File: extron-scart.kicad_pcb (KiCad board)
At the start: 2 copper layers, 17 x 61 mm, 6 parts, among them J1 SCART-F, J2 Conn_Coaxial, J3 Conn_Coaxial, J4 Conn_Coaxial, J5 Conn_Coaxial, J6 Conn_01x03_Male

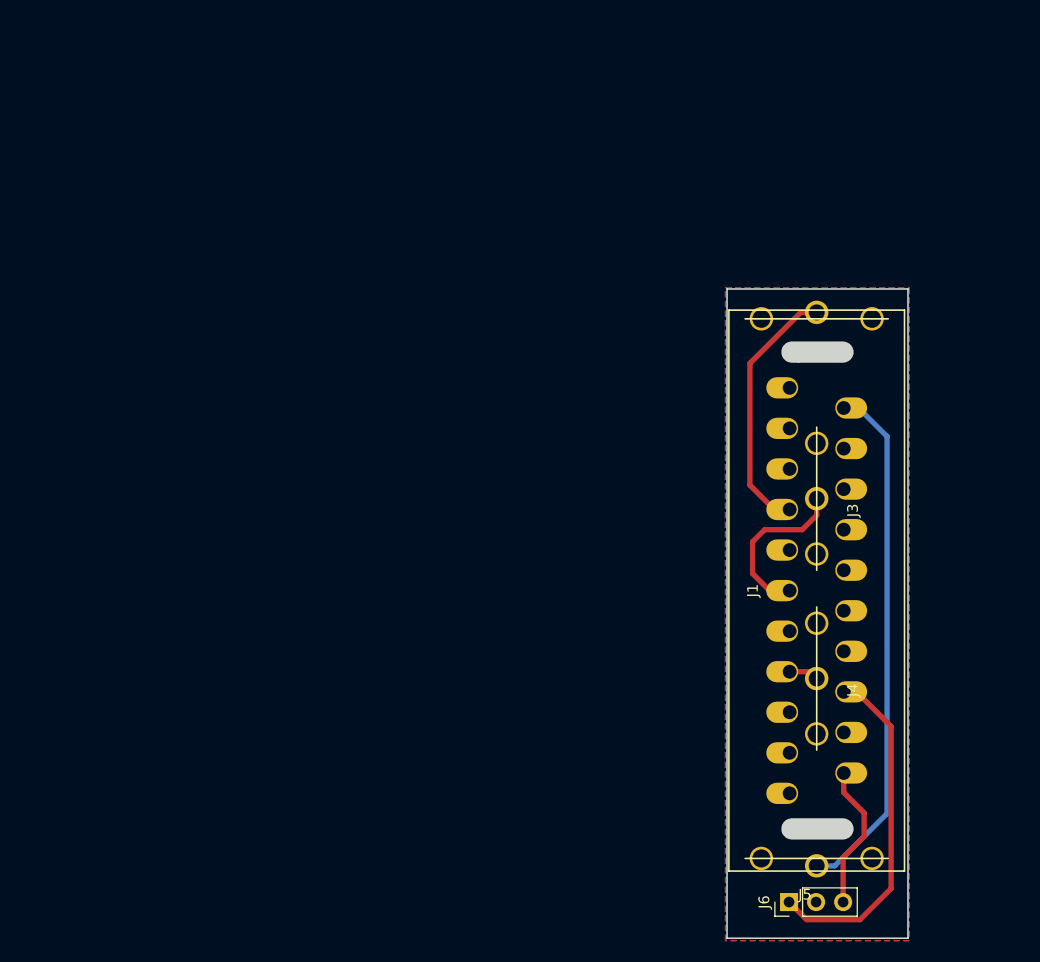
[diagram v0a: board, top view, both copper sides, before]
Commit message: New sch/pcb input from extron crosspoint dimensions
Different orientation for the board
Added selectable sync stripper

Missing mounting holes, and better silkscreen, but mostly done
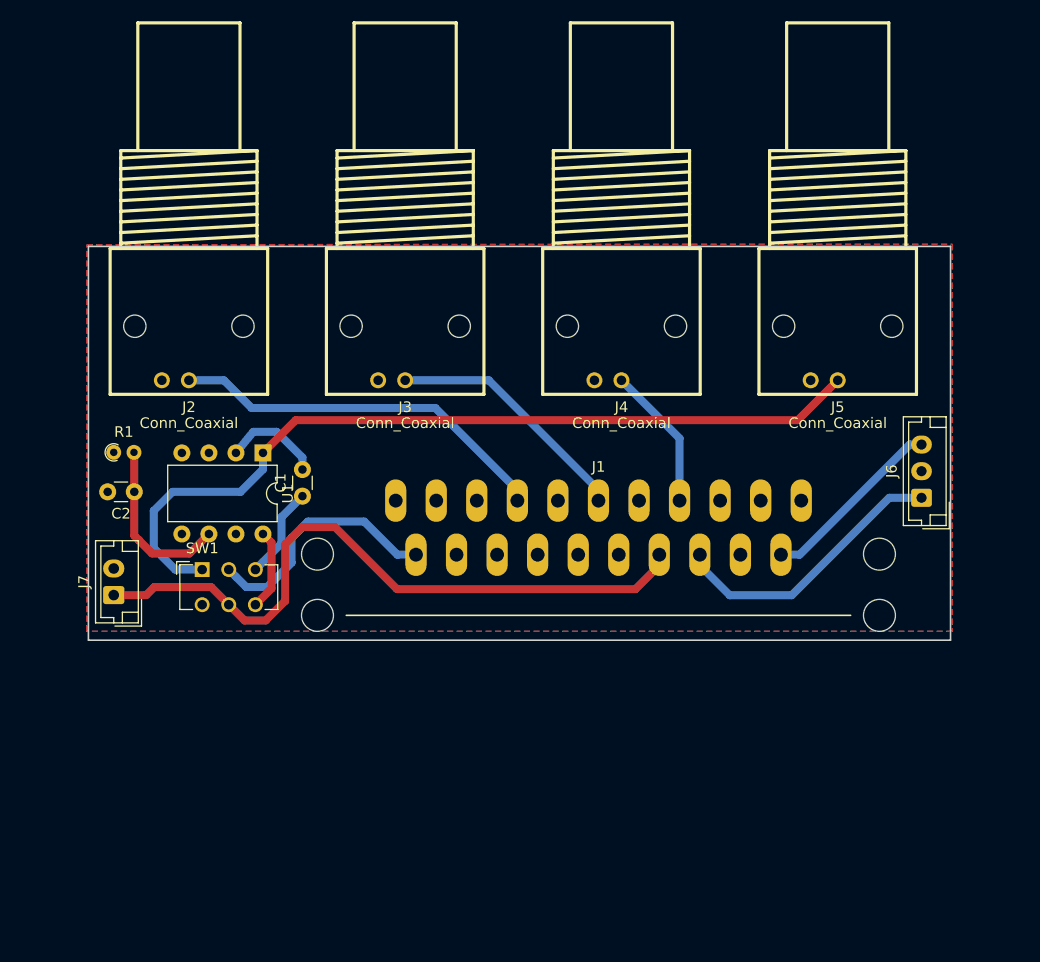
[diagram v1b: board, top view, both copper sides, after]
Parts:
- added C1: 0.1uF, Capacitor_THT:C_Disc_D3.0mm_W1.6mm_P2.50mm, F.Cu at (102.1, 99.5)
- added C2: 0.1uF, Capacitor_THT:C_Disc_D3.0mm_W1.6mm_P2.50mm, F.Cu at (86.3, 99.1)
- added J7: Conn_01x02_Male, Connector_JST:JST_EH_B02B-EH-A_1x02_P2.50mm_Vertical, F.Cu at (84.4, 108.8)
- added R1: 680, Resistor_THT:R_Axial_DIN0204_L3.6mm_D1.6mm_P1.90mm_Vertical, F.Cu at (84.4, 95.4)
- added SW1: SW_DPDT_x2, Button_Switch_THT:SW_CuK_JS202011AQN_DPDT_Angled, F.Cu at (92.7, 106.4)
- added U1: LM1881, Package_DIP:DIP-8_W7.62mm, F.Cu at (98.4, 95.4)
- J1: footprint extron-scart:SCART_F -> extron-scart:SCART_F_RA
- J2, J3, J4, J5: footprint extron-scart:RCA -> extron-scart:BNC_90
- J6: footprint Connector_PinHeader_2.54mm:PinHeader_1x03_P2.54mm_Vertical -> Connector_JST:JST_EH_B03B-EH-A_1x03_P2.50mm_Vertical
- moved J2 59.4 mm to (91.4, 76.2), turned to 180 degrees
- moved J5 57.3 mm to (152.4, 76.2), turned to 180 degrees
- moved J3 45.2 mm to (111.8, 76.2), turned to 180 degrees
- moved J4 44.4 mm to (132.1, 76.2), turned to 180 degrees
- moved J6 40.0 mm to (160.3, 99.6)
- moved J1 20.8 mm to (129.9, 105.0), turned to 180 degrees
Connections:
- net L_AUD renamed Net-(J1-Pad6)
- net R_AUD renamed Net-(J1-Pad2)
- J1 pad 14: Net-(J1-Pad14) -> GND
- J1 pad 20: SYNC -> Net-(J1-Pad20)
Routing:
- net Net-(J1-Pad8): track 0.00 -> 64.0 mm
- net SYNC: track 50.5 -> 79.1 mm
- net Net-(J1-Pad20): track 0.00 -> 23.5 mm
- net Net-(C2-Pad1): track 0.00 -> 16.6 mm
- net RED: track 25.9 -> 36.1 mm
- net Net-(C1-Pad2): track 0.00 -> 9.32 mm
- net BLUE: track 4.27 -> 13.6 mm
- net Net-(C1-Pad1): track 0.00 -> 8.73 mm
- net GREEN: track 15.7 -> 23.4 mm
- net Net-(SW1-Pad6): track 0.00 -> 7.60 mm
- net Net-(J1-Pad6): track 33.3 -> 26.8 mm
- net Net-(J1-Pad2): track 13.7 -> 17.5 mm
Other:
- board size 17 x 61 mm -> 81 x 37 mm

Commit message: V1.0 -> Sent to JLCPCB
Hopefully everything is right
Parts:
- added J10: Conn_01x01, MountingHole:MountingHole_3.2mm_M3, F.Cu at (80.0, 80.0)
- added J11: Conn_01x01, MountingHole:MountingHole_3.2mm_M3, F.Cu at (80.0, 109.0)
- added J8: SENSE, MountingHole:MountingHole_3.2mm_M3, F.Cu at (164.0, 80.0)
- added J9: Conn_01x01, MountingHole:MountingHole_3.2mm_M3, F.Cu at (164.0, 109.0)
- J2: value Conn_Coaxial -> RED
- J3: value Conn_Coaxial -> GREEN
- J4: value Conn_Coaxial -> BLUE
- J5: value Conn_Coaxial -> SYNC
- J6: value Conn_01x03_Male -> PHOENIX; footprint Connector_JST:JST_EH_B03B-EH-A_1x03_P2.50mm_Vertical -> Connector_JST:JST_EH_S03B-EH_1x03_P2.50mm_Horizontal
- J7: value Conn_01x02_Male -> SENSE; footprint Connector_JST:JST_EH_B02B-EH-A_1x02_P2.50mm_Vertical -> Connector_JST:JST_EH_S02B-EH_1x02_P2.50mm_Horizontal
- R1: value 680 -> 680KΩ
- moved J7 81.0 mm to (162.5, 87.5), turned to 270 degrees
- moved C1 16.5 mm to (86.4, 104.4), turned to 180 degrees
- moved U1 4.32 mm to (101.6, 92.5)
- moved J6 3.44 mm to (162.5, 97.0), turned to 270 degrees
- moved SW1 2.62 mm to (90.9, 108.3)
- moved R1 1.27 mm to (84.4, 94.1)
- moved C2 0.71 mm to (86.3, 98.3)
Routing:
- net Net-(J1-Pad8): track 64.0 -> 92.0 mm
- net Net-(J1-Pad2): track 17.5 -> 31.1 mm
- net Net-(C1-Pad2): track 9.32 -> 20.1 mm
- net Net-(SW1-Pad6): track 7.60 -> 15.0 mm
- net SYNC: track 79.1 -> 74.5 mm
- net Net-(J1-Pad6): track 26.8 -> 30.4 mm
- net Net-(C1-Pad1): track 8.73 -> 11.8 mm
- net Net-(C2-Pad1): track 16.6 -> 15.3 mm
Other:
- board size 81 x 37 mm -> 92 x 37 mm
- net class Default: trace_width 0.25 -> 0.254; via_dia 0.6 -> 0.762; via_drill 0.4 -> 0.701
- rule trace_min: 0.2 -> 0.254
- rule via_min_drill: 0.3 -> 0.701
- rule via_min_size: 0.4 -> 0.254
- board text added: "LM1881"
- board text added: "OFF"
- board text added: "ON"
- board text added: "SYNC STRIPPER"
